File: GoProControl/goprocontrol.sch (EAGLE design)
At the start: 17 parts, among them Q1 IRLML6344

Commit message: v0.1 release
Fixed outline for term block and labled pins
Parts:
- U$4: value PTSA-1.5/4-3.5F -> PTSA-1.5/4-3.5F4-3.5IP-2; device synfinatic:PTSA-1.5/4-3.5F -> synfinatic:PTSA-1.5/4-3.5F4-3.5IP-2
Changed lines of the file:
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@@
 <part name="R3" library="Seeed-OPL-Resistor" deviceset="SMD-RES-1K-5%-1/8W(0805)" device="" value="1K"/>
 <part name="SUPPLY8" library="SparkFun-Aesthetics" deviceset="3.3V" device=""/>
-<part name="U$4" library="synfinatic" deviceset="PTSA-1.5/4-3.5F" device=""/>
+<part name="U$4" library="synfinatic" deviceset="PTSA-1.5/4-3.5F" device="4-3.5IP-2" value="PTSA-1.5/4-3.5F4-3.5IP-2"/>
 </parts>
 <sheets>

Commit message: v0.2 small tweaks
- trim board to better fit case
- verify all DRC/ERC
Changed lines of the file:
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@@
 <wire x1="60.96" y1="25.4" x2="60.96" y2="20.32" width="0.1524" layer="91"/>
 <wire x1="60.96" y1="20.32" x2="53.34" y2="20.32" width="0.1524" layer="91"/>
+<junction x="53.34" y="20.32"/>
 </segment>
 <segment>
@@
 <wire x1="40.64" y1="-27.94" x2="40.64" y2="-33.02" width="0.1524" layer="91"/>
 <pinref part="GND4" gate="1" pin="GND"/>
+<junction x="40.64" y="-27.94"/>
 </segment>
 </net>
@@
 <wire x1="127" y1="-2.54" x2="127" y2="-12.7" width="0.1524" layer="91"/>
 <pinref part="C2" gate="G$1" pin="2"/>
+<junction x="127" y="-12.7"/>
 </segment>
 <segment>
@@
 <wire x1="7.62" y1="53.086" x2="7.62" y2="55.88" width="0.1524" layer="91"/>
 <junction x="7.62" y="55.88"/>
+<junction x="12.7" y="55.88"/>
 </segment>
 <segment>
@@
 <pinref part="SUPPLY2" gate="+12V" pin="+12V"/>
 <pinref part="C1" gate="G$1" pin="2"/>
+<junction x="93.98" y="-12.7"/>
 </segment>
 <segment>
@@
 <wire x1="111.76" y1="60.96" x2="127" y2="60.96" width="0.1524" layer="91"/>
 <label x="121.92" y="60.96" size="1.778" layer="95"/>
+<junction x="111.76" y="60.96"/>
 </segment>
 <segment>
@@
 </sheet>
 </sheets>
+<errors>
+</errors>
 </schematic>
 </drawing>

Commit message: v0.4 fix diode pads
My old sod-323 and sod-123 pads always seemed a bit wrong/too small
these new pads are better.
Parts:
- D2: device synfinatic:SCHOTTKY-DIODESOD-323 -> synfinatic:SCHOTTKY-DIODE
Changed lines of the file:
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@@
 <part name="GND3" library="SparkFun" deviceset="GND" device=""/>
 <part name="R4" library="Seeed-OPL-Resistor" deviceset="SMD-RES-1K-5%-1/8W(0805)" device="" value="1K"/>
-<part name="D2" library="synfinatic" deviceset="SCHOTTKY-DIODE" device="SOD-323" value="B5817WS"/>
+<part name="D2" library="synfinatic" deviceset="SCHOTTKY-DIODE" device="" value="B5817WS"/>
 <part name="SUPPLY6" library="SparkFun-Aesthetics" deviceset="3.3V" device=""/>
 <part name="SUPPLY7" library="supply2" deviceset="+12V" device=""/>

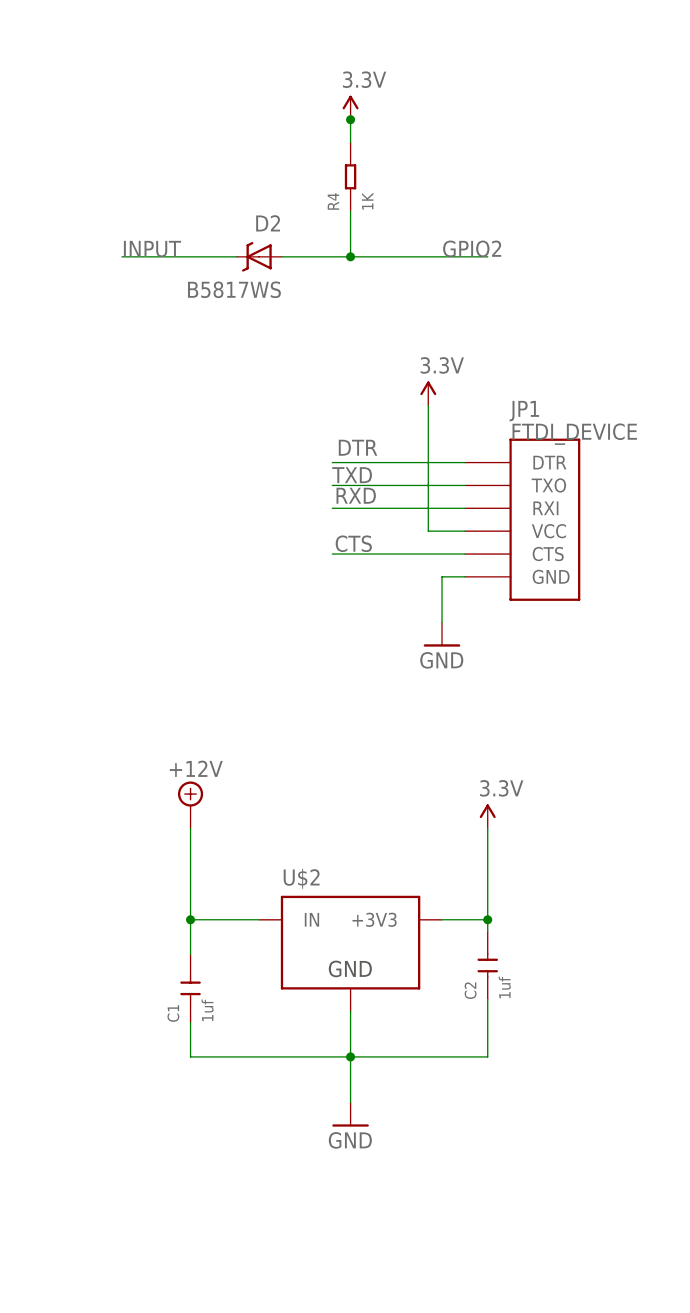
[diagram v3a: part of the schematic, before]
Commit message: Add a 500ma PTC fuse to protect things
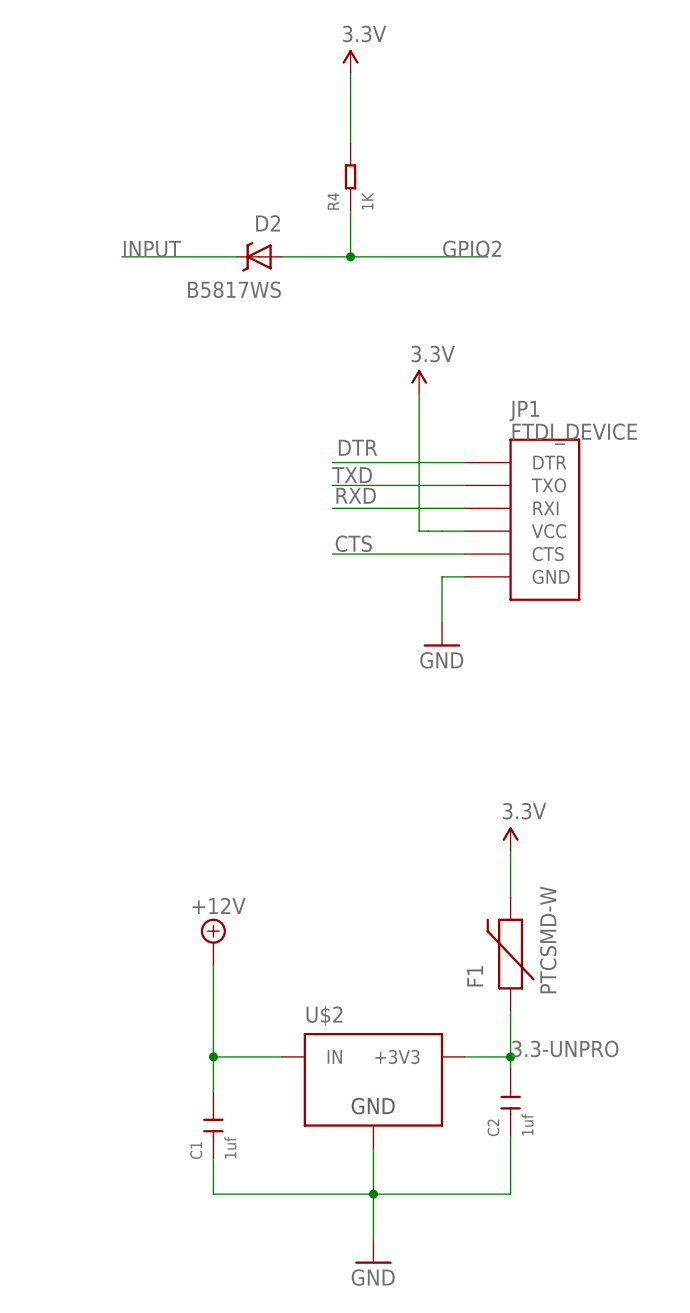
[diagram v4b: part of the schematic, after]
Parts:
- added F1: PTCSMD-W, SparkFun-PowerIC:PTCSMD-W
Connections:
- new net 3.3-UNPRO: C2.2, F1.1, U$2.+3V3
- net 3.3V: now also F1.2; no longer C2.2, U$2.+3V3
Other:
- moved on the sheet: C1, C2, U$2
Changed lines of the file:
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@@
 <part name="SUPPLY3" library="SparkFun-Aesthetics" deviceset="3.3V" device=""/>
 <part name="GND2" library="SparkFun" deviceset="GND" device=""/>
-<part name="SUPPLY4" library="SparkFun-Aesthetics" deviceset="3.3V" device=""/>
 <part name="GND3" library="SparkFun" deviceset="GND" device=""/>
 <part name="R4" library="Seeed-OPL-Resistor" deviceset="SMD-RES-1K-5%-1/8W(0805)" device="" value="1K"/>
@@
 <part name="SUPPLY8" library="SparkFun-Aesthetics" deviceset="3.3V" device=""/>
 <part name="U$4" library="synfinatic" deviceset="PTSA-1.5/4-3.5F" device="4-3.5IP-2" value="PTSA-1.5/4-3.5F4-3.5IP-2"/>
+<part name="F1" library="SparkFun-PowerIC" deviceset="PTC" device="SMD-W"/>
+<part name="SUPPLY4" library="SparkFun-Aesthetics" deviceset="3.3V" device=""/>
 </parts>
 <sheets>
@@
 <instances>
 <instance part="U$1" gate="G$1" x="30.48" y="45.72" rot="R180"/>
-<instance part="U$2" gate="G$1" x="111.76" y="-15.24" smashed="yes">
-<attribute name="NAME" x="104.14" y="-8.89" size="1.778" layer="95"/>
+<instance part="U$2" gate="G$1" x="114.3" y="-30.48" smashed="yes">
+<attribute name="NAME" x="106.68" y="-24.13" size="1.778" layer="95"/>
 </instance>
-<instance part="C1" gate="G$1" x="93.98" y="-20.32" rot="R90"/>
-<instance part="C2" gate="G$1" x="127" y="-17.78" rot="R90"/>
-<instance part="SUPPLY1" gate="G$1" x="127" y="-2.54"/>
-<instance part="GND1" gate="1" x="111.76" y="-35.56"/>
+<instance part="C1" gate="G$1" x="96.52" y="-35.56" rot="R90"/>
+<instance part="C2" gate="G$1" x="129.54" y="-33.02" rot="R90"/>
+<instance part="SUPPLY1" gate="G$1" x="129.54" y="-5.08"/>
+<instance part="GND1" gate="1" x="114.3" y="-50.8"/>
 <instance part="Q1" gate="G$1" x="-43.18" y="58.42"/>
 <instance part="R5" gate="G$1" x="-53.34" y="68.58" rot="R90"/>
@@
 <instance part="D1" gate="G$1" x="-53.34" y="45.72" rot="R90"/>
 <instance part="GND13" gate="1" x="-48.26" y="38.1"/>
-<instance part="SUPPLY2" gate="+12V" x="93.98" y="0"/>
+<instance part="SUPPLY2" gate="+12V" x="96.52" y="-15.24"/>
 <instance part="S1" gate="G$1" x="7.62" y="27.94" rot="R90"/>
 <instance part="S2" gate="G$1" x="60.96" y="30.48" rot="R90"/>
@@
 <instance part="SUPPLY3" gate="G$1" x="12.7" y="58.42"/>
 <instance part="GND2" gate="1" x="33.02" y="15.24"/>
-<instance part="SUPPLY4" gate="G$1" x="120.396" y="44.45"/>
 <instance part="GND3" gate="1" x="121.92" y="17.78"/>
 <instance part="R4" gate="G$1" x="111.76" y="69.85" rot="R90"/>
 <instance part="D2" gate="D$1" x="101.6" y="60.96" rot="R180"/>
-<instance part="SUPPLY6" gate="G$1" x="111.76" y="76.2"/>
+<instance part="SUPPLY6" gate="G$1" x="111.76" y="81.28"/>
 <instance part="SUPPLY7" gate="+12V" x="-22.86" y="15.24"/>
 <instance part="JP1" gate="G$1" x="129.54" y="33.02"/>
@@
 <instance part="SUPPLY8" gate="G$1" x="55.88" y="0"/>
 <instance part="U$4" gate="G$1" x="-43.18" y="0" rot="R180"/>
+<instance part="F1" gate="G$1" x="129.54" y="-17.78" rot="R90"/>
+<instance part="SUPPLY4" gate="G$1" x="119.38" y="45.72"/>
 </instances>
 <busses>
@@
 <net name="GND" class="0">
 <segment>
-<wire x1="127" y1="-21.59" x2="127" y2="-27.94" width="0.1524" layer="91"/>
-<wire x1="93.98" y1="-24.13" x2="93.98" y2="-27.94" width="0.1524" layer="91"/>
-<wire x1="93.98" y1="-27.94" x2="111.76" y2="-27.94" width="0.1524" layer="91"/>
+<wire x1="129.54" y1="-36.83" x2="129.54" y2="-43.18" width="0.1524" layer="91"/>
+<wire x1="96.52" y1="-39.37" x2="96.52" y2="-43.18" width="0.1524" layer="91"/>
+<wire x1="96.52" y1="-43.18" x2="114.3" y2="-43.18" width="0.1524" layer="91"/>
 <pinref part="U$2" gate="G$1" pin="GND"/>
-<wire x1="127" y1="-27.94" x2="111.76" y2="-27.94" width="0.1524" layer="91"/>
-<wire x1="111.76" y1="-27.94" x2="111.76" y2="-22.86" width="0.1524" layer="91"/>
-<wire x1="111.76" y1="-27.94" x2="111.76" y2="-33.02" width="0.1524" layer="91"/>
+<wire x1="129.54" y1="-43.18" x2="114.3" y2="-43.18" width="0.1524" layer="91"/>
+<wire x1="114.3" y1="-43.18" x2="114.3" y2="-38.1" width="0.1524" layer="91"/>
+<wire x1="114.3" y1="-43.18" x2="114.3" y2="-48.26" width="0.1524" layer="91"/>
 <pinref part="GND1" gate="1" pin="GND"/>
 <pinref part="C1" gate="G$1" pin="1"/>
 <pinref part="C2" gate="G$1" pin="1"/>
-<junction x="111.76" y="-27.94"/>
+<junction x="114.3" y="-43.18"/>
 </segment>
 <segment>
@@
 <net name="3.3V" class="2">
 <segment>
-<pinref part="U$2" gate="G$1" pin="+3V3"/>
-<wire x1="121.92" y1="-12.7" x2="127" y2="-12.7" width="0.1524" layer="91"/>
-<wire x1="127" y1="-12.7" x2="127" y2="-13.97" width="0.1524" layer="91"/>
-<pinref part="SUPPLY1" gate="G$1" pin="3.3V"/>
-<wire x1="127" y1="-2.54" x2="127" y2="-12.7" width="0.1524" layer="91"/>
-<pinref part="C2" gate="G$1" pin="2"/>
-<junction x="127" y="-12.7"/>
-</segment>
-<segment>
 <pinref part="U$1" gate="G$1" pin="VCC"/>
 <wire x1="15.24" y1="45.72" x2="12.7" y2="45.72" width="0.1524" layer="91"/>
@@
 </segment>
 <segment>
-<wire x1="124.46" y1="30.48" x2="120.396" y2="30.48" width="0.1524" layer="91"/>
-<wire x1="120.396" y1="30.48" x2="120.396" y2="44.45" width="0.1524" layer="91"/>
-<pinref part="SUPPLY4" gate="G$1" pin="3.3V"/>
-<pinref part="JP1" gate="G$1" pin="VCC"/>
-</segment>
-<segment>
 <pinref part="R4" gate="G$1" pin="2"/>
-<wire x1="111.76" y1="73.66" x2="111.76" y2="76.2" width="0.1524" layer="91"/>
 <pinref part="SUPPLY6" gate="G$1" pin="3.3V"/>
-<wire x1="111.76" y1="76.2" x2="111.76" y2="76.454" width="0.1524" layer="91"/>
-<junction x="111.76" y="76.2"/>
+<wire x1="111.76" y1="73.66" x2="111.76" y2="81.28" width="0.1524" layer="91"/>
 </segment>
 <segment>
@@
 <pinref part="SUPPLY8" gate="G$1" pin="3.3V"/>
 </segment>
+<segment>
+<pinref part="F1" gate="G$1" pin="2"/>
+<pinref part="SUPPLY1" gate="G$1" pin="3.3V"/>
+<wire x1="129.54" y1="-10.16" x2="129.54" y2="-5.08" width="0.1524" layer="91"/>
+</segment>
+<segment>
+<wire x1="124.46" y1="30.48" x2="121.92" y2="30.48" width="0.1524" layer="91"/>
+<pinref part="JP1" gate="G$1" pin="VCC"/>
+<wire x1="121.92" y1="30.48" x2="120.396" y2="30.48" width="0.1524" layer="91"/>
+<wire x1="120.396" y1="30.48" x2="119.38" y2="30.48" width="0.1524" layer="91"/>
+<wire x1="119.38" y1="30.48" x2="119.38" y2="45.72" width="0.1524" layer="91"/>
+<pinref part="SUPPLY4" gate="G$1" pin="3.3V"/>
+</segment>
 </net>
 <net name="+12V" class="1">
@@
 <segment>
 <pinref part="U$2" gate="G$1" pin="IN"/>
-<wire x1="101.6" y1="-12.7" x2="93.98" y2="-12.7" width="0.1524" layer="91"/>
-<wire x1="93.98" y1="-12.7" x2="93.98" y2="-16.51" width="0.1524" layer="91"/>
-<wire x1="93.98" y1="-2.54" x2="93.98" y2="-12.7" width="0.1524" layer="91"/>
+<wire x1="104.14" y1="-27.94" x2="96.52" y2="-27.94" width="0.1524" layer="91"/>
+<wire x1="96.52" y1="-27.94" x2="96.52" y2="-31.75" width="0.1524" layer="91"/>
+<wire x1="96.52" y1="-17.78" x2="96.52" y2="-27.94" width="0.1524" layer="91"/>
 <pinref part="SUPPLY2" gate="+12V" pin="+12V"/>
 <pinref part="C1" gate="G$1" pin="2"/>
-<junction x="93.98" y="-12.7"/>
+<junction x="96.52" y="-27.94"/>
 </segment>
 <segment>
@@
 </segment>
 </net>
+<net name="3.3-UNPRO" class="2">
+<segment>
+<pinref part="U$2" gate="G$1" pin="+3V3"/>
+<wire x1="124.46" y1="-27.94" x2="129.54" y2="-27.94" width="0.1524" layer="91"/>
+<wire x1="129.54" y1="-27.94" x2="129.54" y2="-29.21" width="0.1524" layer="91"/>
+<pinref part="C2" gate="G$1" pin="2"/>
+<pinref part="F1" gate="G$1" pin="1"/>
+<wire x1="129.54" y1="-27.94" x2="129.54" y2="-22.86" width="0.1524" layer="91"/>
+<junction x="129.54" y="-27.94"/>
+<label x="129.54" y="-27.94" size="1.778" layer="95"/>
+</segment>
+</net>

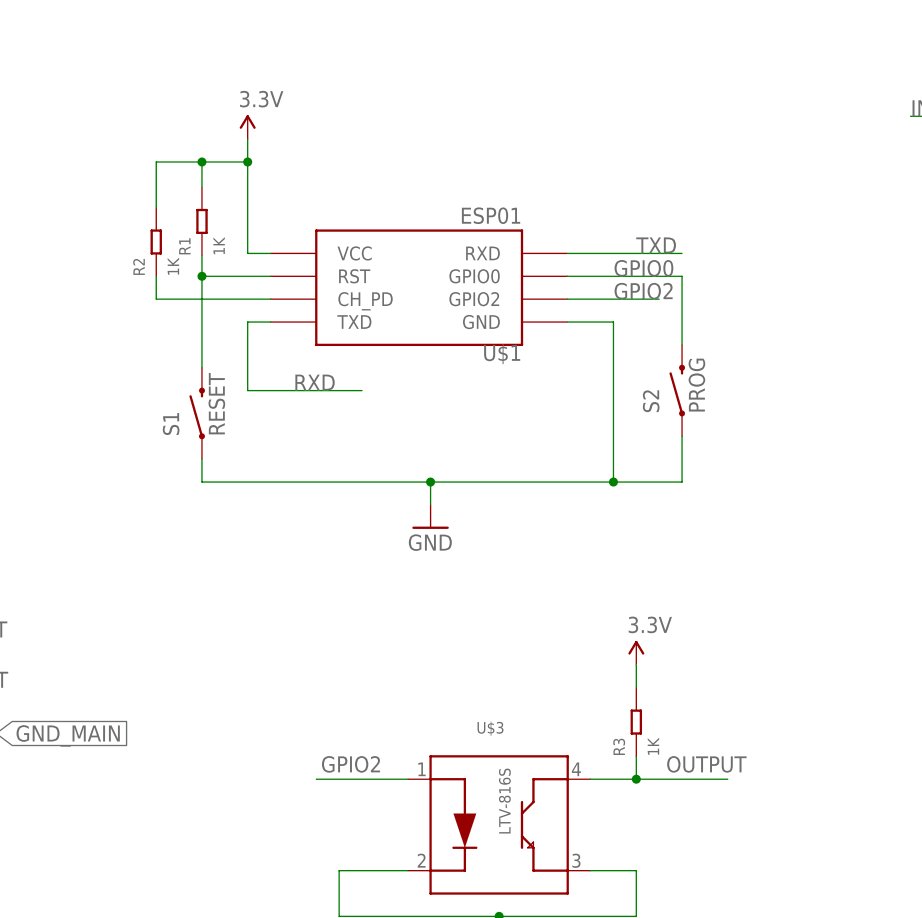
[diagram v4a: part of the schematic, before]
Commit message: Add pullup on GPIO0 for better reliability and switch to 10K pullups
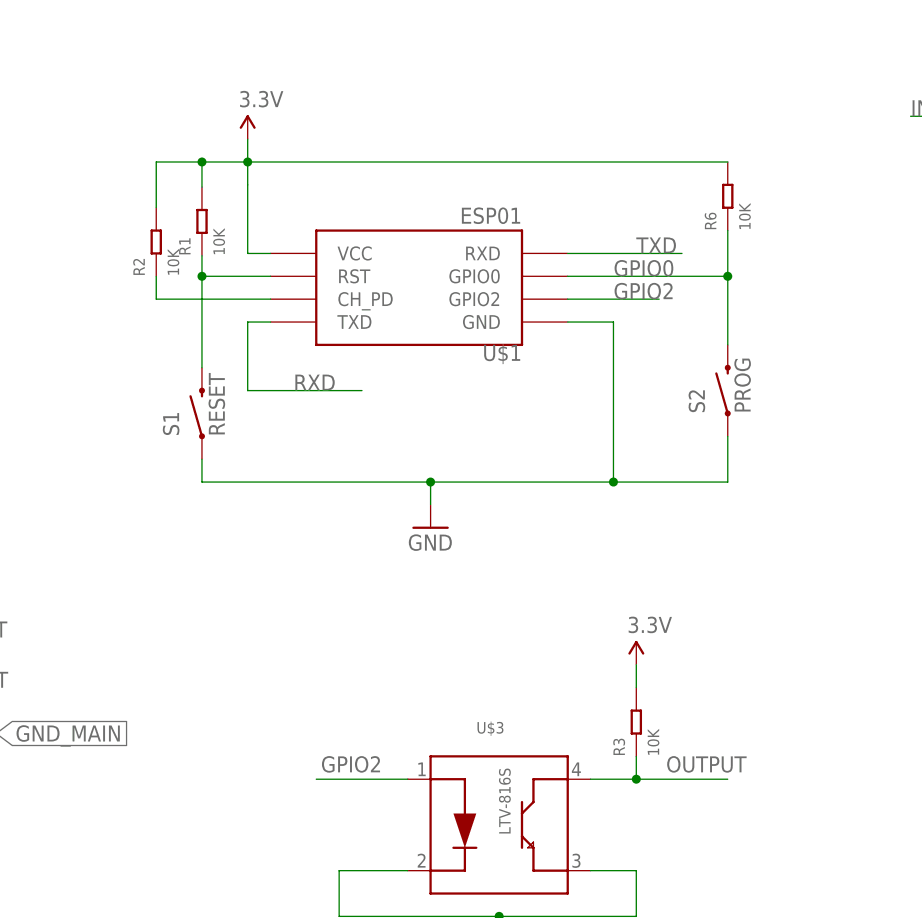
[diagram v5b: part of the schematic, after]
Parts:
- added R6: 10K, Seeed-OPL-Resistor:SMD-RES-10K-1%-1/8W(0805)
- R1, R2, R3: value 1K -> 10K; device Seeed-OPL-Resistor:SMD-RES-1K-5%-1/8W(0805) -> Seeed-OPL-Resistor:SMD-RES-10K-1%-1/8W(0805)
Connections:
- net 3.3V: now also R6.2
- net GPIO0: now also R6.1
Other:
- moved on the sheet: S2
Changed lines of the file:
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@@
 <part name="S1" library="SparkFun-Electromechanical" deviceset="SWITCH-MOMENTARY-2" device="PTH" value="RESET"/>
 <part name="S2" library="SparkFun-Electromechanical" deviceset="SWITCH-MOMENTARY-2" device="PTH" value="PROG"/>
-<part name="R1" library="Seeed-OPL-Resistor" deviceset="SMD-RES-1K-5%-1/8W(0805)" device="" value="1K"/>
-<part name="R2" library="Seeed-OPL-Resistor" deviceset="SMD-RES-1K-5%-1/8W(0805)" device="" value="1K"/>
+<part name="R1" library="Seeed-OPL-Resistor" deviceset="SMD-RES-10K-1%-1/8W(0805)" device="" value="10K"/>
+<part name="R2" library="Seeed-OPL-Resistor" deviceset="SMD-RES-10K-1%-1/8W(0805)" device="" value="10K"/>
 <part name="SUPPLY3" library="SparkFun-Aesthetics" deviceset="3.3V" device=""/>
 <part name="GND2" library="SparkFun" deviceset="GND" device=""/>
@@
 <part name="U$3" library="Seeed-OPL-Transistor" deviceset="SMD-PHOTOCOUPLER-5KV-LTV-816S(4P-4.6X6.5MM)" device="" value="LTV-816S"/>
 <part name="GND4" library="SparkFun" deviceset="GND" device=""/>
-<part name="R3" library="Seeed-OPL-Resistor" deviceset="SMD-RES-1K-5%-1/8W(0805)" device="" value="1K"/>
+<part name="R3" library="Seeed-OPL-Resistor" deviceset="SMD-RES-10K-1%-1/8W(0805)" device="" value="10K"/>
 <part name="SUPPLY8" library="SparkFun-Aesthetics" deviceset="3.3V" device=""/>
 <part name="U$4" library="synfinatic" deviceset="PTSA-1.5/4-3.5F" device="4-3.5IP-2" value="PTSA-1.5/4-3.5F4-3.5IP-2"/>
 <part name="F1" library="SparkFun-PowerIC" deviceset="PTC" device="SMD-W"/>
 <part name="SUPPLY4" library="SparkFun-Aesthetics" deviceset="3.3V" device=""/>
+<part name="R6" library="Seeed-OPL-Resistor" deviceset="SMD-RES-10K-1%-1/8W(0805)" device="" value="10K"/>
 </parts>
 <sheets>
@@
 <instance part="SUPPLY2" gate="+12V" x="96.52" y="-15.24"/>
 <instance part="S1" gate="G$1" x="7.62" y="27.94" rot="R90"/>
-<instance part="S2" gate="G$1" x="60.96" y="30.48" rot="R90"/>
+<instance part="S2" gate="G$1" x="66.04" y="30.48" rot="R90"/>
 <instance part="R1" gate="G$1" x="7.62" y="49.276" rot="R90"/>
 <instance part="R2" gate="G$1" x="2.54" y="46.99" rot="R90"/>
@@
 <instance part="F1" gate="G$1" x="129.54" y="-17.78" rot="R90"/>
 <instance part="SUPPLY4" gate="G$1" x="119.38" y="45.72"/>
+<instance part="R6" gate="G$1" x="66.04" y="52.07" rot="R90"/>
 </instances>
 <busses>
@@
 <junction x="33.02" y="20.32"/>
 <pinref part="S2" gate="G$1" pin="1"/>
-<wire x1="60.96" y1="25.4" x2="60.96" y2="20.32" width="0.1524" layer="91"/>
-<wire x1="60.96" y1="20.32" x2="53.34" y2="20.32" width="0.1524" layer="91"/>
+<wire x1="66.04" y1="25.4" x2="66.04" y2="20.32" width="0.1524" layer="91"/>
+<wire x1="66.04" y1="20.32" x2="53.34" y2="20.32" width="0.1524" layer="91"/>
 <junction x="53.34" y="20.32"/>
 </segment>
@@
 <wire x1="15.24" y1="45.72" x2="12.7" y2="45.72" width="0.1524" layer="91"/>
 <pinref part="SUPPLY3" gate="G$1" pin="3.3V"/>
-<wire x1="12.7" y1="45.72" x2="12.7" y2="55.88" width="0.1524" layer="91"/>
+<wire x1="12.7" y1="45.72" x2="12.7" y2="53.34" width="0.1524" layer="91"/>
 <pinref part="R2" gate="G$1" pin="2"/>
 <wire x1="12.7" y1="55.88" x2="12.7" y2="58.42" width="0.1524" layer="91"/>
@@
 <junction x="7.62" y="55.88"/>
 <junction x="12.7" y="55.88"/>
+<pinref part="R6" gate="G$1" pin="2"/>
+<wire x1="66.04" y1="55.88" x2="12.7" y2="55.88" width="0.1524" layer="91"/>
+<wire x1="12.7" y1="55.88" x2="12.7" y2="53.34" width="0.1524" layer="91"/>
 </segment>
 <segment>
@@
 <pinref part="U$1" gate="G$1" pin="GPIO0"/>
 <pinref part="S2" gate="G$1" pin="2"/>
-<wire x1="48.26" y1="43.18" x2="60.96" y2="43.18" width="0.1524" layer="91"/>
-<wire x1="60.96" y1="43.18" x2="60.96" y2="35.56" width="0.1524" layer="91"/>
+<wire x1="48.26" y1="43.18" x2="66.04" y2="43.18" width="0.1524" layer="91"/>
+<wire x1="66.04" y1="43.18" x2="66.04" y2="35.56" width="0.1524" layer="91"/>
 <label x="53.34" y="43.18" size="1.778" layer="95"/>
-</segment>
-</net>
+<pinref part="R6" gate="G$1" pin="1"/>
+<wire x1="66.04" y1="43.18" x2="66.04" y2="48.26" width="0.1524" layer="91"/>
+<junction x="66.04" y="43.18"/>
+</segment>
+</net>
